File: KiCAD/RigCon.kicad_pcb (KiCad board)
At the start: 2 copper layers, 35.8 x 77 mm, 85 parts, among them J1 USB_C_Receptacle_USB2.0_16P, J2 PJ-320A, J3 PJ-320A, Q1 MMBT5551L, Q2 MMBT5551L, U1 UC EXPANSION, U10 USBLC6-2P6, U11 CH334P, U2 Speaker, U3 Speaker, U4 CP2102N-A02-GQFN24, U5 CM108B, U6 ADM3101E, U7 PCF8523T, U9 TPS2553-1, Y1 12MHz, Y3 32,768 kHz

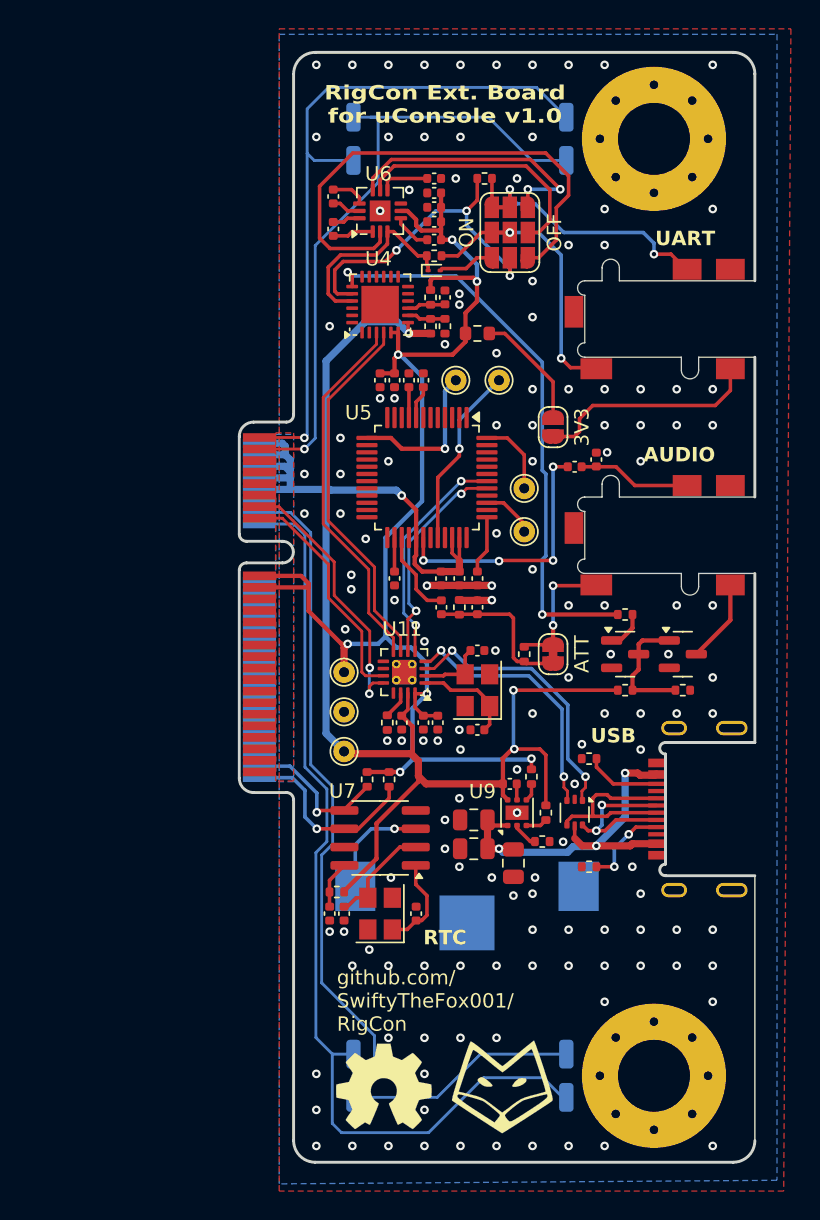
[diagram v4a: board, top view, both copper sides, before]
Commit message: Changes from RigCon version 1.0 to 1.1:
- changed clock crystal footprint
- removed I2C pullup resistor footprints (was DNP before)
- removed unneccessary load caps for clock crystal (RTC has internal ones)
- changed cap value on CM108B pin 37 to 10uF (NECESSARY!)
- removed GND connectrio on CM108B pin 16 SDIN (optional, simplified)

Added directory FrontPanel/ with dxf, openSCAD and stl files
Added Schematic to main dir
Added Render Pic of PCB to main dir
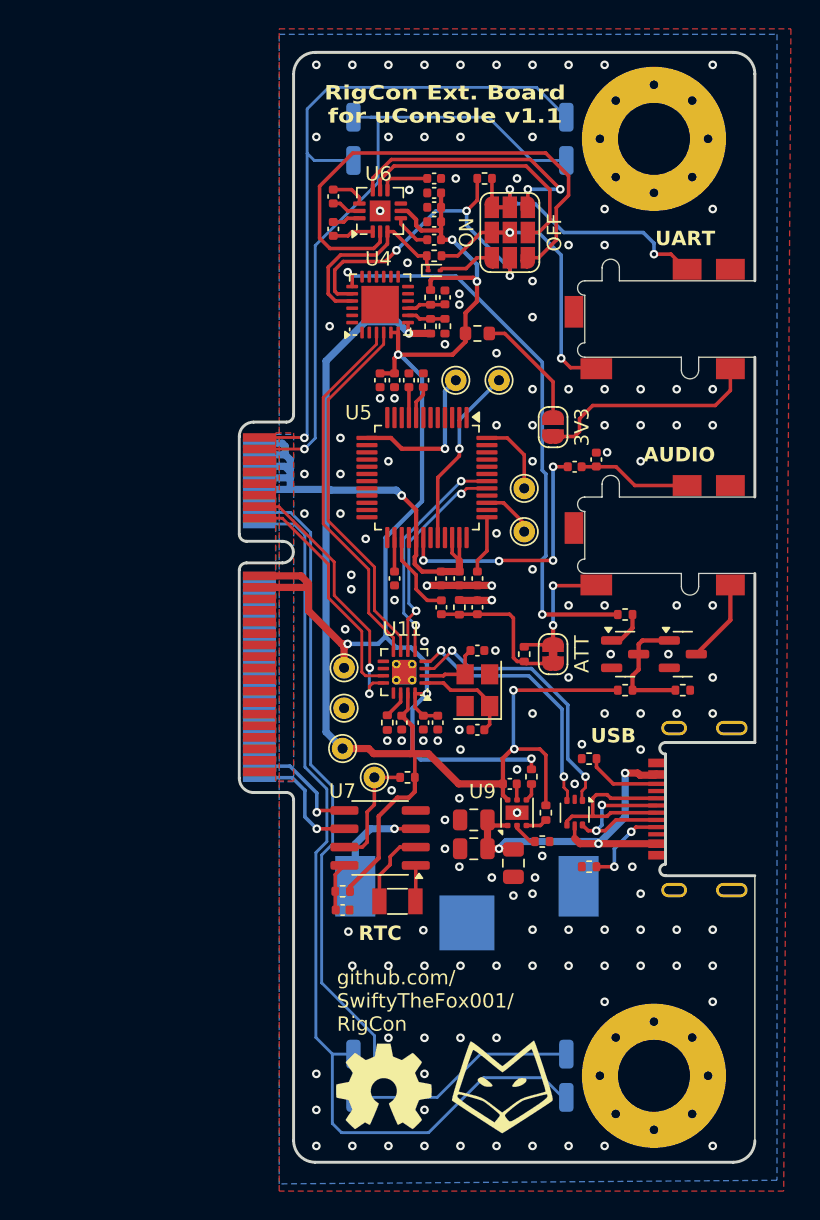
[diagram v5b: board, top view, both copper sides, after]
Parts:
- removed C25, C26: 10pF, Capacitor_SMD:C_0402_1005Metric
- removed R20, R21: DNP, Resistor_SMD:R_0402_1005Metric
- removed Y3: 32,768 kHz, Crystal:Crystal_SMD_3225-4Pin_3.2x2.5mm
- added R8: 22k, Resistor_SMD:R_0402_1005Metric, F.Cu at (107.9, 111.8)
- added TP8: CLK, TestPoint:TestPoint_THTPad_D1.5mm_Drill0.7mm, F.Cu at (105.6, 111.8)
- added Y2: 32,768 kHz, Crystal:Crystal_SMD_3215-2Pin_3.2x1.5mm, F.Cu at (107.2, 120.4)
- moved C30 0.93 mm to (103.4, 121.0), turned to 0 degrees
- moved R7 0.40 mm to (103.4, 119.7)
- moved TP7 0.30 mm to (103.5, 104.2)
- moved TP6 0.25 mm to (103.5, 107.0)
- moved TP1 0.22 mm to (103.4, 109.8)
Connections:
- U7 pad 7: unconnected-(U7-~{INT1}/CLKOUT-Pad7) -> Net-(U7-~{INT1}/CLKOUT)
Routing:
- net Net-(U7-~{INT1}/CLKOUT): track 0.00 -> 8.21 mm
- net /GPIO45_SCL0: track 13.2 -> 8.44 mm
- net +3V3: track 95.3 -> 91.2 mm, vias 7 -> 6
- net Net-(U7-OSCI): track 6.59 -> 2.51 mm
- net /GPIO44_SDA0: track 10.4 -> 8.13 mm
- net Net-(U7-OSCO): track 7.45 -> 5.46 mm
- net +5V: track 119.9 -> 121.2 mm
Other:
- board text added: "RigCon Ext. Board for uConsole v1.1"
- board text removed: "Cut: half circle 1.5d, line 3 Connector is at the center Length*Width 25.7*3.75"
- board text removed: "RigCon Ext. Board for uConsole v1.0"
- board text removed: "Speaker is on B.Cu This one on the left is Left(original U5)"
- board text removed: "Speaker is on B.Cu This one on the left is Right(original U6)"

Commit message: PCB: Minor Changes Updated Document Information (Header, Version, Date)
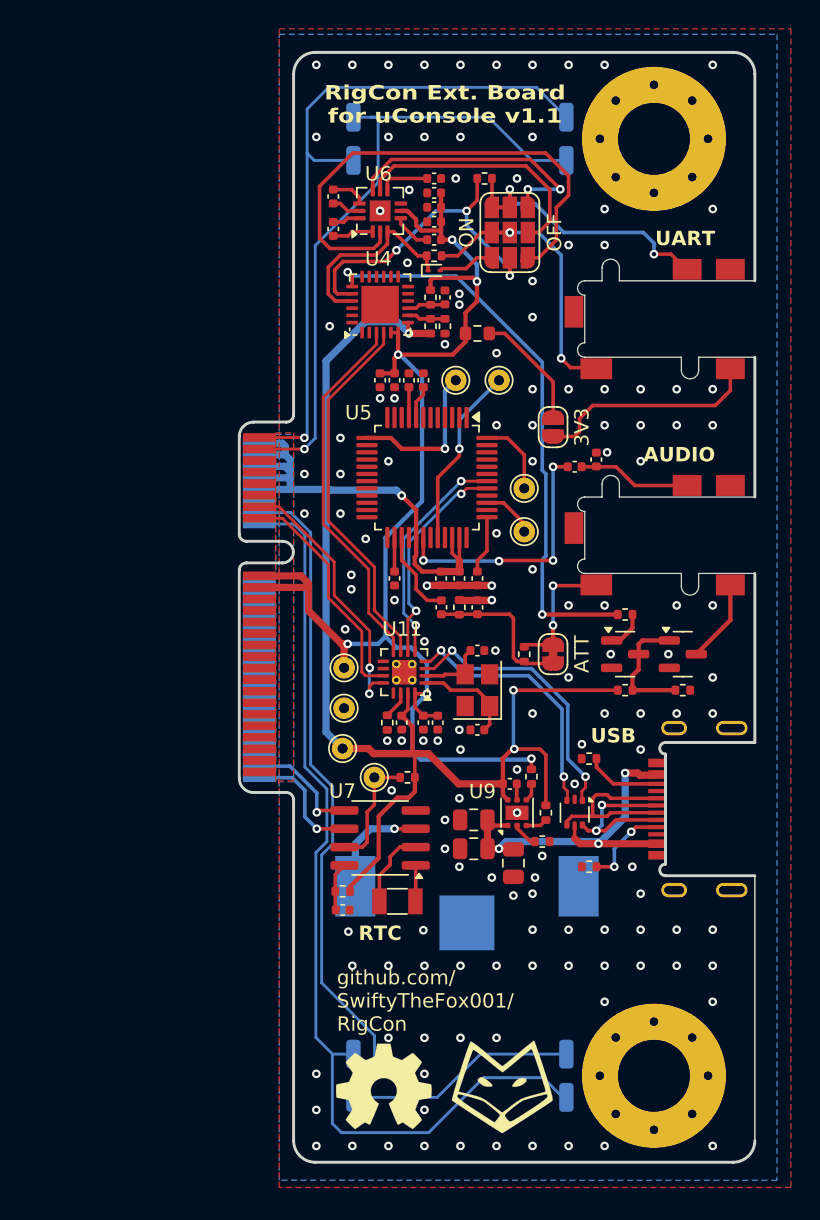
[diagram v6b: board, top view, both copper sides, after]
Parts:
- C17: value 100nF -> 10uF
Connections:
- U5 pad 16: GND -> unconnected-(U5-SDIN-Pad16)
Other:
- board text added: "RigCon Extension Board"
- board text added: "for Clockwork PI uConsole"
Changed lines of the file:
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@@
 	(title_block
 		(title "RigCon Extension Board for ClockworkPi uConsole")
-		(date "2025-02-26")
-		(rev "1.0")
+		(date "2025-03-22")
+		(rev "1.1")
 	)
 	(layers
@@
 	(net 161 "unconnected-(H2-Pad1)_7")
 	(net 162 "unconnected-(H2-Pad1)_8")
+	(net 163 "unconnected-(U5-SDIN-Pad16)")
 	(footprint "Package_SO:SOIC-8_3.9x4.9mm_P1.27mm"
 		(layer "F.Cu")
@@
 			)
 		)
-		(property "Value" "100nF"
+		(property "Value" "10uF"
 			(at 0 1.16 90)
 			(layer "F.Fab")
@@
 			(layers "F.Cu" "F.Paste" "F.Mask")
 			(roundrect_rratio 0.25)
-			(net 16 "GND")
+			(net 163 "unconnected-(U5-SDIN-Pad16)")
 			(pinfunction "SDIN")
-			(pintype "input")
+			(pintype "input+no_connect")
 		)
 		(pad "17" smd roundrect
@@
 		)
 	)
+	(gr_text "for Clockwork PI uConsole"
+		(at 179 179.25 0)
+		(layer "Cmts.User")
+		(effects
+			(font
+				(size 2.5 2.5)
+				(thickness 0.25)
+			)
+			(justify left bottom)
+		)
+	)
 	(gr_text "F.Cu faces the back cover(rear)\nB.Cu faces the LCD(front)"
 		(at 158 103 0)
@@
 		)
 	)
+	(gr_text "RigCon Extension Board"
+		(at 178.5 173.25 0)
+		(layer "Cmts.User")
+		(effects
+			(font
+				(size 4 4)
+				(thickness 0.5)
+			)
+			(justify left bottom)
+		)
+	)
 	(dimension
 		(type aligned)
@@
 		(polygon
 			(pts
-				(xy 99 59.868) (xy 134.5 59.868) (xy 134 140.5) (xy 99 140.5)
+				(xy 99 59.868) (xy 134.5 59.868) (xy 134.5 140.25) (xy 99 140.25)
 			)
 		)
@@
 		(polygon
 			(pts
-				(xy 99 60.252) (xy 133.536 60.25) (xy 133.536 139.751) (xy 99 140)
+				(xy 99 60.252) (xy 133.536 60.25) (xy 133.536 139.751) (xy 99 139.75)
 			)
 		)
